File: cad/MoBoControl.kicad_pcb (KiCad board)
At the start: 2 copper layers, 100 x 58 mm, 64 parts, among them J101 Conn_01x03, J102 Conn_01x03, J103 Conn_01x03, J104 Conn_01x03, J105 Conn_01x03, J106 Conn_01x03, J107 Conn_01x03, J108 Conn_02x05_Odd_Even, J109 Conn_01x02, J110 Conn_01x02, J111 Conn_01x04, J112 USB_A, J113 Conn_02x05_Odd_Even, J114 power_input, J115 RPi_GPIO, J116 Conn_02x10_Odd_Even, U101 ASSR-1218, U102 ASSR-1218, U103 ASSR-1218, U104 ASSR-1218, U105 ASSR-1218, U106 ASSR-1218, U107 ASSR-1218, U108 ASSR-1218, U109 ASSR-1218, U110 ASSR-1218, U111 ASSR-1218, U112 ASSR-1218, U113 ASSR-1218, U114 ASSR-1218, U115 ASSR-1218, U116 ASSR-1218, U117 MCP23017

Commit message: rev1 cleanup
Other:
- board text added: "MoBoControl v1.0 github.com/mithro/MoBoControl"
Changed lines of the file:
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@@
     (fp_line (start 5.72 15.26) (end -3.18 15.26)
       (stroke (width 0.1) (type solid)) (layer "F.Fab"))
-    (pad "1" thru_hole roundrect (at 0 0 270) (size 1.7 1.7) (drill 1) (layers "*.Cu" "*.Mask") (roundrect_rratio 0.147059)
+    (pad "1" thru_hole roundrect (at 0 0 270) (size 1.7 1.7) (drill 1) (layers "*.Cu" "*.Mask") (roundrect_rratio 0.1470588235)
       (net 68 "unconnected-(J108-Pin_1-Pad1)") (pinfunction "Pin_1") (pintype "passive"))
     (pad "2" thru_hole circle (at 2.54 0 270) (size 1.7 1.7) (drill 1) (layers "*.Cu" "*.Mask")
@@
     (property "Sheetname" "")
     (attr through_hole)
-    (fp_text reference "J115" (at 1.27 -2.33 90) (layer "F.SilkS")
+    (fp_text reference "J115" (at 1.27 -2.33 90) (layer "F.SilkS") hide
         (effects (font (size 1 1) (thickness 0.15)))
     )
@@
     (effects (font (size 1.5 1.5) (thickness 0.3) bold) (justify bottom mirror))
   )
+  (gr_text "MoBoControl v1.0\ngithub.com/mithro/MoBoControl" (at 74.73 39.04) (layer "B.SilkS")
+    (effects (font (size 2.5 2.5) (thickness 0.5) bold) (justify left bottom mirror))
+  )
   (gr_text locked "PWR\n" (at 15 9 90) (layer "F.SilkS")
     (effects (font (size 1.2 1.22) (thickness 0.3) bold) (justify left bottom))
@@
     (effects (font (size 1 1) (thickness 0.25) bold) (justify left bottom))
   )
+  (gr_text "MoBoControl v1.0\ngithub.com/mithro/MoBoControl" (at 19.09 45.77) (layer "F.SilkS")
+    (effects (font (size 2.5 2.5) (thickness 0.5) bold) (justify left bottom))
+  )
   (gr_text "SDA" (at 100.94 11.29 -90) (layer "F.SilkS")

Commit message: Mobo V2 sent off for production
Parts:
- removed the J109 at (14.1, 0.50)
- added C103: 22uF, Capacitor_SMD:C_0805_2012Metric, F.Cu at (89.3, 8.11)
- added C104: .1uF, Capacitor_SMD:C_0603_1608Metric, F.Cu at (102.3, 8.59)
- added C105: .1uF, Capacitor_SMD:C_0603_1608Metric, F.Cu at (100.8, 7.83)
- added C106: .1uF, Capacitor_SMD:C_0603_1608Metric, F.Cu at (91.3, 9.84)
- added C107: .1uF, Capacitor_SMD:C_0603_1608Metric, F.Cu at (101.1, 4.83)
- added C108: .1uF, Capacitor_SMD:C_0603_1608Metric, F.Cu at (101.6, 2.56)
- added H101: MountingHole, MountingHole:MountingHole_3.2mm_M3_DIN965, F.Cu at (21.0, -5.72)
- added H102: MountingHole, MountingHole:MountingHole_3.2mm_M3_DIN965, F.Cu at (97.0, -5.72)
- added H103: MountingHole, MountingHole:MountingHole_3.2mm_M3_DIN965, F.Cu at (97.0, 56.0)
- added H104: MountingHole, MountingHole:MountingHole_3.2mm_M3_DIN965, F.Cu at (21.0, 56.0)
- added J105: Conn_02x04_Odd_Even, Connector_PinHeader_2.54mm:PinHeader_2x04_P2.54mm_Vertical, F.Cu at (9.59, -6.49)
- added J112: Conn_02x03_Odd_Even, Connector_PinHeader_2.54mm:PinHeader_2x03_P2.54mm_Vertical, F.Cu at (79.0, 40.0)
- added J117: Conn_01x15, Connector_PinSocket_2.54mm:PinSocket_1x15_P2.54mm_Vertical, F.Cu at (64.1, 32.0)
- added J118: Conn_01x15, Connector_PinSocket_2.54mm:PinSocket_1x15_P2.54mm_Vertical, F.Cu at (64.1, 57.4)
- added R134: 4.7k, Resistor_SMD:R_0603_1608Metric, F.Cu at (9.68, 51.1)
- added R135: 4.7k, Resistor_SMD:R_0603_1608Metric, F.Cu at (9.68, 49.5)
- added R136: 4.7k, Resistor_SMD:R_0603_1608Metric, F.Cu at (60.2, 42.6)
- added R137: 4.7k, Resistor_SMD:R_0603_1608Metric, F.Cu at (62.0, 42.6)
- added R138: 4.7k, Resistor_SMD:R_0603_1608Metric, F.Cu at (63.8, 42.6)
- added R139: 4.7k, Resistor_SMD:R_0603_1608Metric, F.Cu at (65.5, 42.6)
- added R140: 4.7k, Resistor_SMD:R_0603_1608Metric, F.Cu at (67.2, 42.8)
- added R141: 4.7k, Resistor_SMD:R_0603_1608Metric, F.Cu at (69.0, 42.8)
- added SW101: SW_Push, Button_Switch_SMD:SWITCH_2x3_SMD_TACTILE_GREEN, F.Cu at (49.0, -7.46)
- added SW102: SW_Push, Button_Switch_SMD:SWITCH_2x3_SMD_TACTILE_GREEN, F.Cu at (33.3, -7.71)
- added U118: MAX232, Package_SO:SOIC-16_3.9x9.9mm_P1.27mm, F.Cu at (96.1, 4.63)
- moved J110 54.1 mm to (9.51, 54.5)
- moved J113 51.7 mm to (82.7, 57.9), turned to 90 degrees
- moved J119 24.2 mm to (73.9, -4.00), turned to 90 degrees
- moved R133 23.1 mm to (71.6, 57.6)
- moved D115 23.1 mm to (71.7, 55.9)
- moved J114 9.65 mm to (89.1, 47.8), turned to 180 degrees
- moved JP101 8.42 mm to (89.9, 53.5), turned to 90 degrees
- moved R142 7.97 mm to (89.6, 53.5), turned to 90 degrees
- moved J111 5.12 mm to (94.3, 46.5), turned to 90 degrees
- moved R143 4.95 mm to (87.5, 53.4), turned to 90 degrees
- moved JP102 4.60 mm to (87.2, 53.5), turned to 90 degrees
- renumbered J102 to J101, J103 to J102, J101 to J103, J107 to J106, J106 to J107, J105 to J108, J114 to J109, J112 to J111, J111 to J113, J113 to J114, J108 to J119, R103 to R101, R104 to R102, R105 to R103, R106 to R104, R101 to R105, R102 to R106, R129 to R117, R121 to R118, R122 to R119, R130 to R120, R119 to R121, R120 to R122, R117 to R123, R118 to R124, R134 to R131, R135 to R132, R132 to R133, R131 to R142, R133 to R143, U103 to U101, U104 to U102, U105 to U103, U106 to U104, U101 to U105, U102 to U106, U115 to U109, U113 to U110, U114 to U111, U116 to U112, U111 to U113, U112 to U114, U109 to U115, U110 to U116
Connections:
- net /IO_SCL renamed /D27
- net /IO_SDA renamed /D26
- net /LAD0 renamed /D19
- net /LAD1 renamed /D23
- net /LAD2 renamed /D15
- net /LAD3 renamed /D32
- net /LCLK renamed /D18
- net /LDRQ renamed /D21
- net /LED renamed /D2
- net /LFRAME renamed /D25
- net /LPCPD renamed /D22
- net /LRESET renamed /D33
- net /SCL renamed /D16
- net /SDA renamed /D4
- net /SER_IRQ renamed /D5
- net /SMB_CLK renamed /D14
- net /SMB_DAT renamed /D17
- J109 pad 2: unconnected-(J114-Pin_2-Pad2) (its old number) -> GND
- J110 pad 2: Net-(J110-Pin_2) -> GND
- J115 pad 10: /RX -> /D13
- J115 pad 17: +3V3 -> unconnected-(J115-3.3V-Pad17)
- J115 pad 27: unconnected-(J115-ID_SD-Pad27) -> /D34
- J115 pad 31: unconnected-(J115-GPIO06-Pad31) -> /D39
- J115 pad 36: unconnected-(J115-GPIO16-Pad36) -> /D36
- J115 pad 7: unconnected-(J115-GPIO04_GCLK-Pad7) -> /D12
- J115 pad 8: /TX -> /D35
- U112 pad 3: Net-(J110-Pin_2) -> Net-(J105-Pin_2)
- U112 pad 4: Net-(J110-Pin_1) -> Net-(J105-Pin_1)
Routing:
- net /D35: track 0.00 -> 101.4 mm, vias 0 -> 2
- net +3V3: track 143.1 -> 241.3 mm
- net /D13: track 0.00 -> 95.4 mm
- net /TX: track 111.2 -> 18.5 mm, vias 2 -> 0
- net /RX: track 104.6 -> 21.5 mm, vias 2 -> 0
- net Net-(J105-Pin_2): track 0.00 -> 70.7 mm
- net Net-(J105-Pin_1): track 0.00 -> 58.9 mm, vias 0 -> 1
- net Net-(J105-Pin_5): track 25.9 -> 77.2 mm
- net /D12: track 0.00 -> 47.9 mm, vias 0 -> 5
- net /D17: track 30.3 -> 72.5 mm, vias 0 -> 4
- net /D15: track 44.5 -> 86.1 mm, vias 0 -> 4
- net /D5: track 24.9 -> 65.4 mm, vias 0 -> 3
- net Net-(J105-Pin_6): track 31.2 -> 67.6 mm, vias 0 -> 2
- net /D21: track 18.0 -> 53.0 mm, vias 0 -> 2
- net /D22: track 11.1 -> 45.2 mm, vias 0 -> 2
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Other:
- board size 100 x 58 mm -> 100 x 70 mm
- board text added: "+"
- board text added: "-"
- board text added: "3v3"
- board text added: "5v"
- board text added: "LED SENS3"
- board text added: "LED_SENS1"
- board text added: "LED_SENS2"
- board text added: "MoBoControl v2.0 github.com/mithro/MoBoControl"
- board text added: "PWR"
- board text added: "RST"
- board text added: "SPKR"
- board text removed: "MoBoControl v1.0 github.com/mithro/MoBoControl"
- board text removed: "RESET"
- board text removed: "locked"

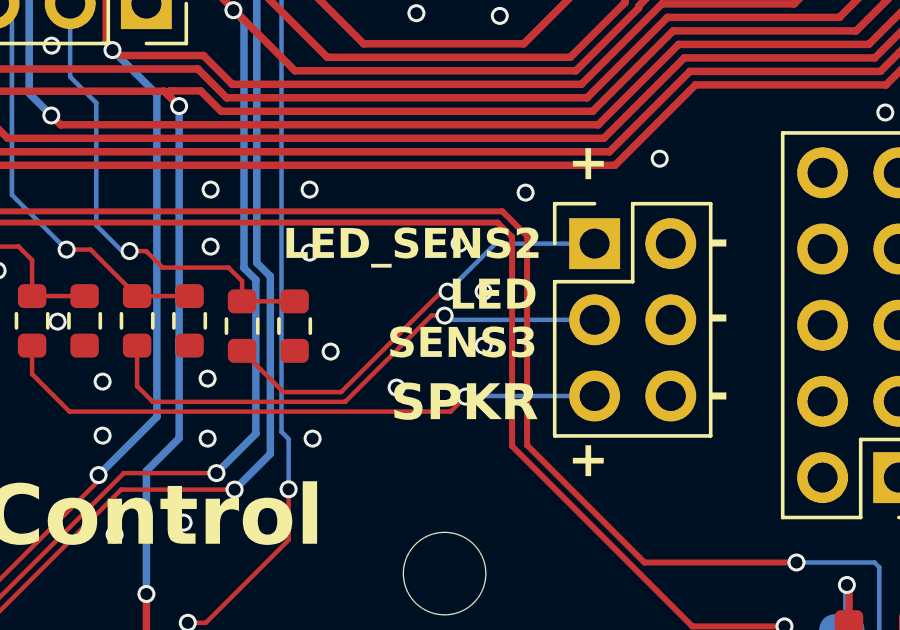
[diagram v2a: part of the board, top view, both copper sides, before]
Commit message: make pdf of schematic
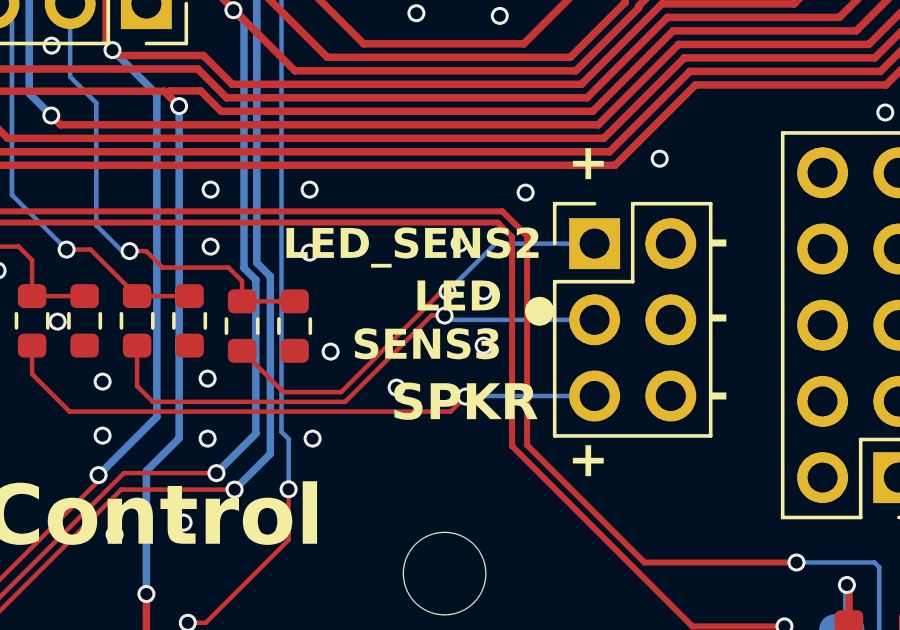
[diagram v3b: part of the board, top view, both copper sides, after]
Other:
- board text added: "•"
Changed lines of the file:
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@@
     (effects (font (size 1.2 1.2) (thickness 0.3) bold))
+  )
+  (gr_text "•" (at 78.04 43.52) (layer "F.SilkS")
+    (effects (font (size 2 2) (thickness 0.5) bold) (justify right bottom))
   )
   (gr_text "SCL" (at 86.86 56.34 90) (layer "F.SilkS")
@@
     (effects (font (size 1.5 1.5) (thickness 0.3) bold) (justify left bottom))
   )
-  (gr_text "LED\nSENS3" (at 77.1 43.9) (layer "F.SilkS")
+  (gr_text "LED\nSENS3" (at 75.92 43.96) (layer "F.SilkS")
     (effects (font (size 1 1) (thickness 0.25) bold) (justify right bottom))
   )

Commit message: gerbers
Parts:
- R101, R102, R103, R104, R105, R106, R107, R108, R117, R118, R119, R120, R121, R122, R123, R124, R133, R134, R135, R136, R137, R138, R139, R140, R141, R142, R143: value 4.7k -> 220R
- renumbered C103 to C102, C102 to C103, J111 to J109, J109 to J110, J116 to J111, J114 to J112, J110 to J113, J117 to J114, J112 to J115, J113 to J116, J118 to J117, J115 to J118, JP103 to JP101, JP101 to JP102, JP102 to JP103
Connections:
- J118 pad 27: /D34 -> /D36
- J118 pad 36: /D36 -> /D34
- R136 pad 2: /D34 -> /D36
- R137 pad 1: /D34 -> /D36
- R140 pad 2: /D36 -> /D34
- R141 pad 1: /D36 -> /D34
